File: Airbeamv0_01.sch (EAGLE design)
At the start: 89 parts

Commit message: minor changes to schematic
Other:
- note added: "TODO: - X Make U_ILIM wider - X Put metal on switch mounting holes - X Power switch has incorrect circuit diagram, fix - X Voltage output is 5.1V -- check out why - X Move Buffer away from BT module - X Make dust connector holes slightly larger - X Flip T+RH Sensor Connections"
- note removed: "TODO: - X Make U_ILIM wider - X Put metal on switch mounting holes - X Power switch has incorrect circuit diagram, fix - X Voltage output is 5.1V -- check out why - X Move Buffer away from BT module - Make dust connector holes slightly larger - Flip T+RH Sensor Connections"
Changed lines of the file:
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@@
 </part>
 <part name="U$25" library="MyPOW" deviceset="VUSB" device=""/>
-<part name="SUPPLY2" library="supply2" deviceset="GND1" device="" value="UGND"/>
 <part name="UC_C2" library="SparkFun-Passives" deviceset="CAP" device="0603-CAP" value="100n">
 <attribute name="PARTNO" value="C1608X7R1E104K080AA"/>
@@
 <attribute name="PARTNO" value="AtMega32U4-XUAU"/>
 </part>
-<part name="SUPPLY1" library="supply2" deviceset="GND1" device="" value="UGND"/>
 <part name="GND4" library="supply1" deviceset="GND" device=""/>
 <part name="GND15" library="supply1" deviceset="GND" device=""/>
@@
 - X Voltage output is 5.1V -- check out why
 - X Move Buffer away from BT module
-- Make dust connector holes slightly larger
-- Flip T+RH Sensor Connections</text>
+- X  Make dust connector holes slightly larger
+- X  Flip T+RH Sensor Connections</text>
 <text x="68.58" y="-55.88" size="3.81" layer="94" ratio="10" rot="MR180" align="top-left">BATTERY</text>
 <text x="-139.7" y="0" size="6.35" layer="94">POWER</text>
@@
 </instance>
 <instance part="U$25" gate="G$1" x="-38.1" y="66.04"/>
-<instance part="SUPPLY2" gate="G$1" x="-53.34" y="38.1"/>
 <instance part="UC_C2" gate="G$1" x="-40.64" y="134.62">
 <attribute name="PARTNO" x="-40.64" y="134.62" size="1.778" layer="96" display="off"/>
@@
 <attribute name="PARTNO" x="175.26" y="104.14" size="1.778" layer="96" display="off"/>
 </instance>
-<instance part="SUPPLY1" gate="G$1" x="-111.76" y="-58.42"/>
 <instance part="GND4" gate="1" x="-38.1" y="43.18"/>
 <instance part="GND15" gate="1" x="-106.68" y="116.84" rot="R270"/>
@@
 <pinref part="GND39" gate="1" pin="GND"/>
 <pinref part="U_C3" gate="G$1" pin="2"/>
+<junction x="-25.4" y="-38.1"/>
 </segment>
 <segment>
@@
 <label x="-53.34" y="43.18" size="1.778" layer="95" rot="R90"/>
 <label x="-53.34" y="63.5" size="1.778" layer="95" rot="R90"/>
-<pinref part="SUPPLY2" gate="G$1" pin="GND1"/>
 <pinref part="U_MEGA32U-Q" gate="G$1" pin="UGND"/>
 <pinref part="UC_R3" gate="G$1" pin="2"/>
@@
 <wire x1="-127" y1="-55.88" x2="-111.76" y2="-55.88" width="0.1524" layer="91"/>
 <wire x1="-111.76" y1="-55.88" x2="-111.76" y2="-43.18" width="0.1524" layer="91"/>
-<junction x="-111.76" y="-55.88"/>
 <label x="-119.38" y="-55.88" size="1.778" layer="95"/>
-<pinref part="SUPPLY1" gate="G$1" pin="GND1"/>
 <pinref part="CON_USB" gate="G$1" pin="T5"/>
 <wire x1="-111.76" y1="-43.18" x2="-121.92" y2="-43.18" width="0.1524" layer="91"/>
@@
 <wire x1="30.48" y1="-17.78" x2="53.34" y2="-17.78" width="0.1524" layer="91"/>
 <junction x="53.34" y="-17.78"/>
+<junction x="66.04" y="-17.78"/>
 </segment>
 </net>
@@
 <junction x="116.84" y="-48.26"/>
 <junction x="134.62" y="-48.26"/>
-</segment>
-<segment>
+<junction x="147.32" y="-22.86"/>
+<junction x="116.84" y="-22.86"/>
+</segment>
+<segment>

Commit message: updating for ordering
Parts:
- ATMEGA32U4-T: PARTNO AtMega32U4-XUAU -> ATMEGA32U4-AU
- CON_EXTERN: PARTNO (none) -> 1770911
- RESET_SWITCH: value SWITCH -> DNP
- U_FANM: value MOSFET-N -> DNP
- renumbered U$1 to U_FANM, U$4 to CON_EXTERN
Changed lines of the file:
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@@
 <parts>
 <part name="CON_ICSP" library="SmartPrj" deviceset="PINHD-2X3" device="" value="ICSP">
-<attribute name="DNP" value=""/>
 <attribute name="PARTNO" value="67997-206HLF "/>
 </part>
@@
 </part>
 <part name="ATMEGA32U4-T" library="SmartPrj" deviceset="ATMEGA32U4-XU" device="AU">
-<attribute name="PARTNO" value="AtMega32U4-XUAU"/>
+<attribute name="PARTNO" value="ATMEGA32U4-AU"/>
 </part>
 <part name="GND4" library="supply1" deviceset="GND" device=""/>
@@
 <part name="GND21" library="supply1" deviceset="GND" device=""/>
 <part name="GND38" library="supply1" deviceset="GND" device=""/>
-<part name="RESET_SWITCH" library="Airbeam" deviceset="SWITCH" device="">
+<part name="RESET_SWITCH" library="Airbeam" deviceset="SWITCH" device="" value="DNP">
 <attribute name="DNP" value=""/>
 </part>
@@
 <attribute name="PARTNO" value="MH2029-600Y"/>
 </part>
-<part name="U$1" library="Airbeam" deviceset="MOSFET-N" device="">
+<part name="U_FANM" library="Airbeam" deviceset="MOSFET-N" device="" value="DNP">
 <attribute name="DNP" value=""/>
 </part>
@@
 <attribute name="PARTNO" value="RC0603JR-0710KL"/>
 </part>
-<part name="U$4" library="Airbeam" deviceset="TBLOCK_5" device=""/>
+<part name="CON_EXTERN" library="Airbeam" deviceset="TBLOCK_5" device="">
+<attribute name="PARTNO" value="1770911"/>
+</part>
 <part name="U_FB3" library="Airbeam" deviceset="FERITE_BEAD" device="">
 <attribute name="PARTNO" value="MH2029-600Y"/>
@@
 <attribute name="VALUE" x="-54.61" y="170.18" size="1.778" layer="96"/>
 <attribute name="PARTNO" x="-58.42" y="165.1" size="1.778" layer="96" display="off"/>
-<attribute name="DNP" x="-58.42" y="165.1" size="1.778" layer="96" display="off"/>
 </instance>
 <instance part="P+1" gate="1" x="-43.18" y="177.8" smashed="yes">
@@
 <attribute name="PARTNO" x="-50.8" y="104.14" size="1.778" layer="96" rot="R90" display="off"/>
 </instance>
-<instance part="U$1" gate="G$1" x="-96.52" y="-162.56" rot="R270">
+<instance part="U_FANM" gate="G$1" x="-96.52" y="-162.56" rot="R270">
 <attribute name="DNP" x="-96.52" y="-162.56" size="1.778" layer="96" rot="R270" display="off"/>
 </instance>
@@
 <attribute name="PARTNO" x="-114.3" y="-134.62" size="1.778" layer="96" rot="R90" display="off"/>
 </instance>
-<instance part="U$4" gate="G$1" x="-127" y="-154.94"/>
+<instance part="CON_EXTERN" gate="G$1" x="-127" y="-154.94">
+<attribute name="PARTNO" x="-127" y="-154.94" size="1.778" layer="96" display="off"/>
+</instance>
 <instance part="U_FB3" gate="G$1" x="-53.34" y="-20.32" rot="R90">
 <attribute name="PARTNO" x="-53.34" y="-20.32" size="1.778" layer="96" rot="R90" display="off"/>
@@
 <wire x1="-134.62" y1="-205.74" x2="-144.78" y2="-205.74" width="0.1524" layer="91"/>
 <junction x="-134.62" y="-205.74"/>
-<pinref part="U$4" gate="G$1" pin="T_4"/>
+<pinref part="CON_EXTERN" gate="G$1" pin="T_4"/>
 <junction x="-124.46" y="-157.48"/>
-<pinref part="U$4" gate="G$1" pin="B_4"/>
+<pinref part="CON_EXTERN" gate="G$1" pin="B_4"/>
 </segment>
 <segment>
@@
 <pinref part="+3V4" gate="G$1" pin="+3V3"/>
 <junction x="-101.6" y="-162.56"/>
-<pinref part="U$1" gate="G$1" pin="P$2"/>
+<pinref part="U_FANM" gate="G$1" pin="P$2"/>
 </segment>
 <segment>
@@
 <pinref part="U_Z5" gate="G$1" pin="1"/>
 <junction x="-127" y="-193.04"/>
-<pinref part="U$4" gate="G$1" pin="T_3"/>
+<pinref part="CON_EXTERN" gate="G$1" pin="T_3"/>
 <junction x="-127" y="-157.48"/>
-<pinref part="U$4" gate="G$1" pin="B_3"/>
+<pinref part="CON_EXTERN" gate="G$1" pin="B_3"/>
 </segment>
 <segment>
@@
 <wire x1="-129.54" y1="-157.48" x2="-129.54" y2="-180.34" width="0.1524" layer="91"/>
 <wire x1="-129.54" y1="-180.34" x2="-144.78" y2="-180.34" width="0.1524" layer="91"/>
-<pinref part="U$4" gate="G$1" pin="T_2"/>
+<pinref part="CON_EXTERN" gate="G$1" pin="T_2"/>
 <junction x="-129.54" y="-157.48"/>
-<pinref part="U$4" gate="G$1" pin="B_2"/>
+<pinref part="CON_EXTERN" gate="G$1" pin="B_2"/>
 </segment>
 <segment>
@@
 <wire x1="-132.08" y1="-157.48" x2="-132.08" y2="-167.64" width="0.1524" layer="91"/>
 <wire x1="-132.08" y1="-167.64" x2="-144.78" y2="-167.64" width="0.1524" layer="91"/>
-<pinref part="U$4" gate="G$1" pin="T_1"/>
+<pinref part="CON_EXTERN" gate="G$1" pin="T_1"/>
 <junction x="-132.08" y="-157.48"/>
-<pinref part="U$4" gate="G$1" pin="B_1"/>
+<pinref part="CON_EXTERN" gate="G$1" pin="B_1"/>
 </segment>
 <segment>
@@
 <wire x1="-96.52" y1="-154.94" x2="-96.52" y2="-160.02" width="0.1524" layer="91"/>
 <label x="-96.52" y="-154.94" size="1.778" layer="95"/>
-<pinref part="U$1" gate="G$1" pin="P$1"/>
+<pinref part="U_FANM" gate="G$1" pin="P$1"/>
 </segment>
 <segment>
@@
 <pinref part="VR_R4" gate="G$1" pin="2"/>
 <wire x1="-91.44" y1="-162.56" x2="-91.44" y2="-172.72" width="0.1524" layer="91"/>
-<pinref part="U$1" gate="G$1" pin="P$3"/>
+<pinref part="U_FANM" gate="G$1" pin="P$3"/>
 <pinref part="U$2" gate="G$1" pin="P1"/>
 <wire x1="-91.44" y1="-162.56" x2="-78.74" y2="-162.56" width="0.1524" layer="91"/>
@@
 <wire x1="-121.92" y1="-220.98" x2="-147.32" y2="-220.98" width="0.1524" layer="91"/>
 <pinref part="CA_FB1" gate="G$1" pin="P$2"/>
-<pinref part="U$4" gate="G$1" pin="T_5"/>
+<pinref part="CON_EXTERN" gate="G$1" pin="T_5"/>
 <junction x="-121.92" y="-157.48"/>
-<pinref part="U$4" gate="G$1" pin="B_5"/>
-</segment>
-</net>
+<pinref part="CON_EXTERN" gate="G$1" pin="B_5"/>
+</segment>
+</net>

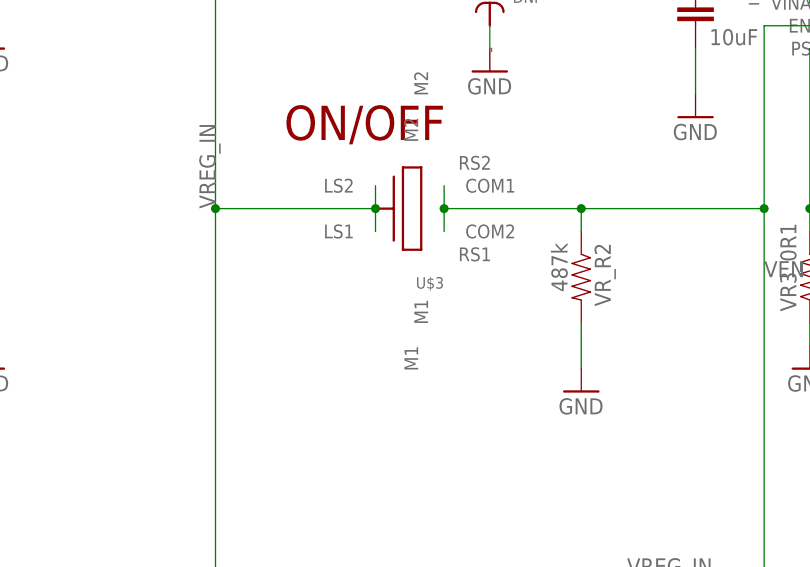
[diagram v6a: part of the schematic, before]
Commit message: BOM updated, board outline modified for cheaper version (per Chris), FINAL
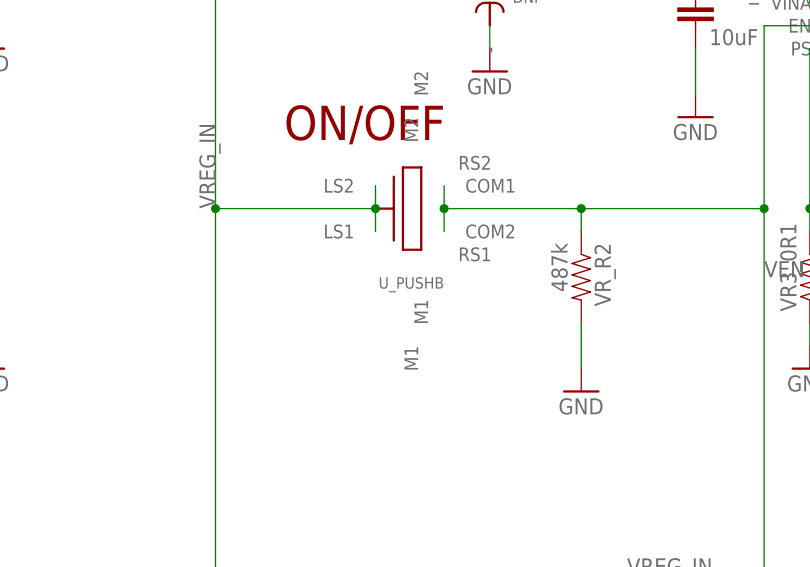
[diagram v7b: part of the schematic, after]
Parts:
- U_MEGA32U-Q: PARTNO DNP -> ATMEGA32U4-MU
- renumbered U$2 to CON_FAN, U$3 to U_PUSHB
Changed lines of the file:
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@@
 <part name="GND3" library="supply1" deviceset="GND" device=""/>
 <part name="U_MEGA32U-Q" library="SmartPrj" deviceset="ATMEGA32U4-XU" device="MU" value="DNP">
-<attribute name="PARTNO" value="DNP"/>
+<attribute name="PARTNO" value="ATMEGA32U4-MU
+"/>
 </part>
 <part name="ATMEGA32U4-T" library="SmartPrj" deviceset="ATMEGA32U4-XU" device="AU">
@@
 <part name="VR_C1" library="Airbeam" deviceset="CAP_POL" device="120UF" value="DNP"/>
 <part name="GND48" library="supply1" deviceset="GND" device=""/>
-<part name="U$2" library="Airbeam" deviceset="SUR_2PIN" device=""/>
+<part name="CON_FAN" library="Airbeam" deviceset="SUR_2PIN" device=""/>
 <part name="CONHEADER_FAN" library="Airbeam" deviceset="PART_OFFBOARD" device="" value="OFF_BOARD">
 <attribute name="PARTNO" value="02SUR-32S"/>
 </part>
-<part name="U$3" library="Airbeam" deviceset="PUSHBUTTON" device=""/>
+<part name="U_PUSHB" library="Airbeam" deviceset="PUSHBUTTON" device=""/>
 <part name="U_USB_CH" library="Airbeam" deviceset="USB-BATTERY_LOAD" device="">
 <attribute name="PARTNO" value="AAT3672IWO-4.2-1-T1"/>
@@
 <instance part="GND3" gate="1" x="129.54" y="48.26"/>
 <instance part="U_MEGA32U-Q" gate="G$1" x="17.78" y="104.14">
-<attribute name="PARTNO" x="17.78" y="104.14" size="6.35" layer="96" display="off"/>
+<attribute name="PARTNO" x="17.78" y="104.14" size="1.778" layer="96" display="off"/>
 </instance>
 <instance part="ATMEGA32U4-T" gate="G$1" x="175.26" y="104.14">
@@
 <instance part="VR_C1" gate="G$1" x="147.32" y="-25.4"/>
 <instance part="GND48" gate="1" x="147.32" y="-33.02"/>
-<instance part="U$2" gate="G$1" x="-76.2" y="-167.64"/>
+<instance part="CON_FAN" gate="G$1" x="-76.2" y="-167.64"/>
 <instance part="CONHEADER_FAN" gate="G$1" x="276.86" y="-38.1">
 <attribute name="PARTNO" x="276.86" y="-38.1" size="1.778" layer="96" display="off"/>
 </instance>
-<instance part="U$3" gate="G$1" x="137.16" y="-48.26" rot="R90"/>
+<instance part="U_PUSHB" gate="G$1" x="137.16" y="-48.26" rot="R90"/>
 <instance part="U_USB_CH" gate="G$1" x="22.86" y="-25.4">
 <attribute name="PARTNO" x="22.86" y="-25.4" size="1.778" layer="96" display="off"/>
@@
 </segment>
 <segment>
-<pinref part="U$2" gate="G$1" pin="P2"/>
+<pinref part="CON_FAN" gate="G$1" pin="P2"/>
 <pinref part="GND14" gate="1" pin="GND"/>
 <wire x1="-73.66" y1="-165.1" x2="-73.66" y2="-162.56" width="0.1524" layer="91"/>
 <wire x1="-73.66" y1="-162.56" x2="-63.5" y2="-162.56" width="0.1524" layer="91"/>
 <wire x1="-63.5" y1="-162.56" x2="-63.5" y2="-180.34" width="0.1524" layer="91"/>
-<pinref part="U$2" gate="G$1" pin="PAD1"/>
+<pinref part="CON_FAN" gate="G$1" pin="PAD1"/>
 <wire x1="-63.5" y1="-180.34" x2="-63.5" y2="-185.42" width="0.1524" layer="91"/>
 <wire x1="-81.28" y1="-170.18" x2="-81.28" y2="-180.34" width="0.1524" layer="91"/>
 <wire x1="-81.28" y1="-180.34" x2="-71.12" y2="-180.34" width="0.1524" layer="91"/>
-<pinref part="U$2" gate="G$1" pin="PAD2"/>
+<pinref part="CON_FAN" gate="G$1" pin="PAD2"/>
 <wire x1="-71.12" y1="-180.34" x2="-71.12" y2="-170.18" width="0.1524" layer="91"/>
 <wire x1="-71.12" y1="-180.34" x2="-63.5" y2="-180.34" width="0.1524" layer="91"/>
@@
 <label x="165.1" y="-22.86" size="1.778" layer="95"/>
 <wire x1="147.32" y1="-22.86" x2="116.84" y2="-22.86" width="0.1524" layer="91"/>
-<pinref part="U$3" gate="G$1" pin="LS1"/>
-<pinref part="U$3" gate="G$1" pin="LS2"/>
+<pinref part="U_PUSHB" gate="G$1" pin="LS1"/>
+<pinref part="U_PUSHB" gate="G$1" pin="LS2"/>
 <wire x1="134.62" y1="-45.72" x2="134.62" y2="-48.26" width="0.1524" layer="91"/>
 <wire x1="134.62" y1="-48.26" x2="134.62" y2="-50.8" width="0.1524" layer="91"/>
@@
 <wire x1="-91.44" y1="-162.56" x2="-91.44" y2="-172.72" width="0.1524" layer="91"/>
 <pinref part="U_FANM" gate="G$1" pin="P$3"/>
-<pinref part="U$2" gate="G$1" pin="P1"/>
+<pinref part="CON_FAN" gate="G$1" pin="P1"/>
 <wire x1="-91.44" y1="-162.56" x2="-78.74" y2="-162.56" width="0.1524" layer="91"/>
 <wire x1="-78.74" y1="-162.56" x2="-78.74" y2="-165.1" width="0.1524" layer="91"/>
@@
 <wire x1="157.48" y1="-48.26" x2="157.48" y2="-50.8" width="0.1524" layer="91"/>
 <pinref part="VR_R2" gate="G$1" pin="1"/>
-<pinref part="U$3" gate="G$1" pin="COM2"/>
-<pinref part="U$3" gate="G$1" pin="COM1"/>
+<pinref part="U_PUSHB" gate="G$1" pin="COM2"/>
+<pinref part="U_PUSHB" gate="G$1" pin="COM1"/>
 <wire x1="142.24" y1="-50.8" x2="142.24" y2="-48.26" width="0.1524" layer="91"/>
 <wire x1="142.24" y1="-48.26" x2="142.24" y2="-45.72" width="0.1524" layer="91"/>

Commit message: updated Gerber
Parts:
- VR5_L1: value 6uH -> 4.7uH; PARTNO RT6150BGQW -> CBC3225T4R7MR
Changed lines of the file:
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@@
 <part name="GND3" library="supply1" deviceset="GND" device=""/>
 <part name="U_MEGA32U-Q" library="SmartPrj" deviceset="ATMEGA32U4-XU" device="MU" value="DNP">
-<attribute name="PARTNO" value="ATMEGA32U4-MU
-"/>
+<attribute name="PARTNO" value="ATMEGA32U4-MU "/>
 </part>
 <part name="ATMEGA32U4-T" library="SmartPrj" deviceset="ATMEGA32U4-XU" device="AU">
@@
 </part>
 <part name="GND22" library="supply1" deviceset="GND" device=""/>
-<part name="VR5_L1" library="SparkFun-Passives" deviceset="INDUCTOR" device="1210" value="6uH">
-<attribute name="PARTNO" value="RT6150BGQW"/>
+<part name="VR5_L1" library="SparkFun-Passives" deviceset="INDUCTOR" device="1210" value="4.7uH">
+<attribute name="PARTNO" value="CBC3225T4R7MR"/>
 </part>
 <part name="P+7" library="supply1" deviceset="+5V" device=""/>
